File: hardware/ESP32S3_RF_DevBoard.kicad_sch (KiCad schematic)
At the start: 0 parts

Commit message: working on first block- usb-c block
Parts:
- added J1: USB4105-GF-A, USB4105-GF-A:GCT_USB4105-GF-A, symbol USB4105-GF-A:USB4105-GF-A
- added R1, R2: 5.1k, symbol Device:R
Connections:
- new net: J1.A5 (CC1), R1.1
- new net: J1.B5 (CC2), R2.1
- new net +5V_USB: J1.A4_B9 (VBUS), J1.B4_A9 (VBUS__1)
- new net GND: J1.A1_B12 (GND), J1.B1_A12 (GND__1), J1.SH1 (SHELL_GND), J1.SH4 (SHELL_GND__3), R1.2, R2.2
- new net USB_D+: J1.A6 (DP1), J1.B6 (DP2)
- new net USB_D-: J1.A7 (DN1), J1.B7 (DN2)
- no-connect marks 0 -> 2

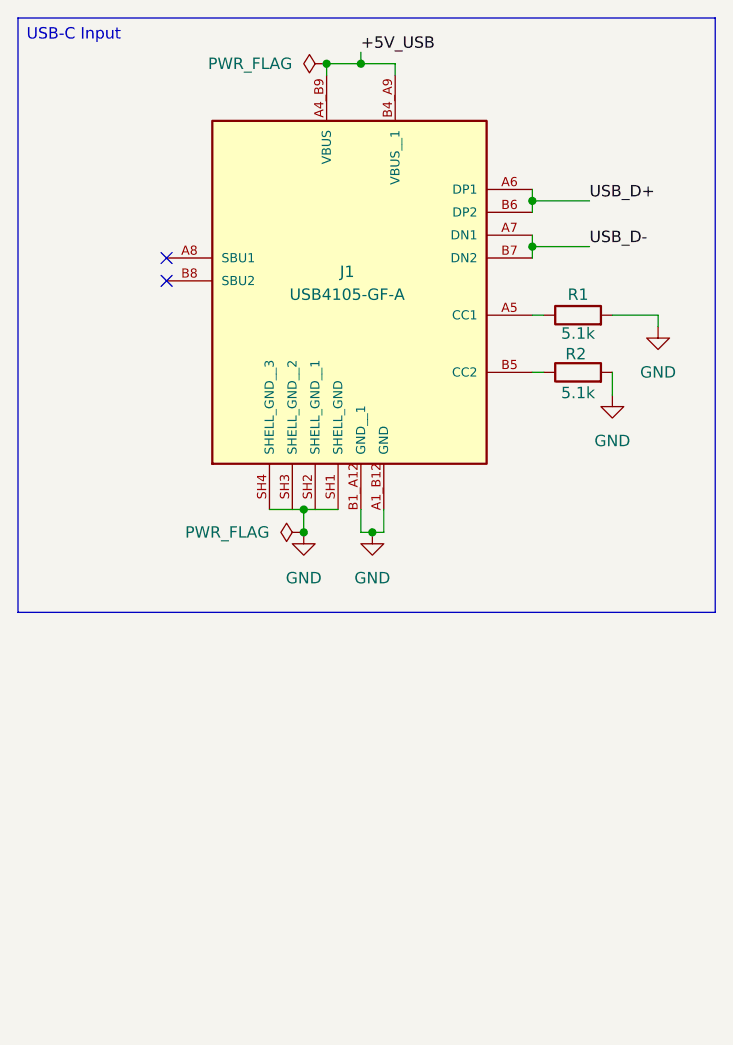
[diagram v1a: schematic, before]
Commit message: working on the USB data ESD blk
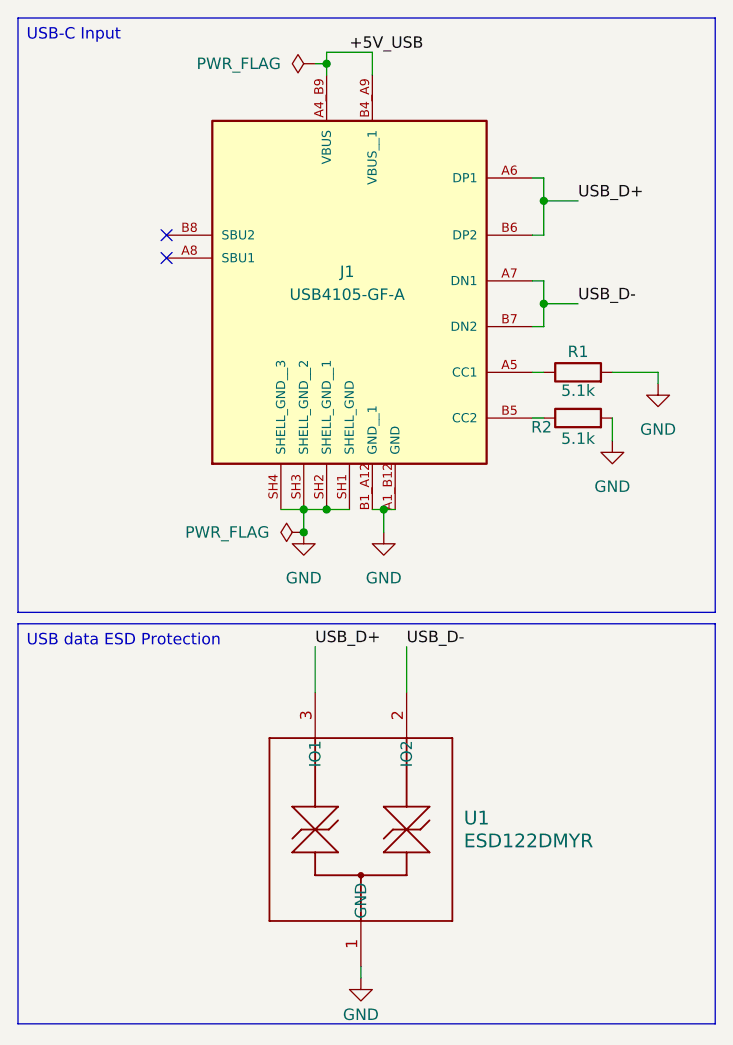
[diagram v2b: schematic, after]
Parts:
- added U1: ESD122DMYR, ESP32S3-RF-DevBoard:DMY0003A, symbol ESD122DMYR:ESD122DMYR
- J1: footprint USB4105-GF-A:GCT_USB4105-GF-A -> ESP32S3-RF-DevBoard:GCT_USB4105-GF-A
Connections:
- net GND: now also J1.SH2 (SHELL_GND__1), J1.SH3 (SHELL_GND__2), U1.1 (GND)
- net USB_D+: now also U1.3 (IO1)
- net USB_D-: now also U1.2 (IO2)
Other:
- moved on the sheet: R1, R2
